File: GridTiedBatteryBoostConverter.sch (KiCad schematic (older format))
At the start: 58 parts, among them J101 Battery Connection, J103 Solar Panels, Q101 IXFP36N20X3, Q102 BC847B-13-F, Q103 SSM3K329R, Q104 SSM3J334R, U101 OPA2837IDGKR, U102 UCC2800DTR

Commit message: Replaced TK32A12N1,S4X TO-220 Toshiba transistors that were use for turning the charger on and off, with a pair of IRFP4321PBF's from Infinion, in a TO-247AC package.  The reson for the change was this part of the circuit carries ~20A at 102.2V peak, so for a 30 degree rise in trace temp with 2 Once copper we need 5mm trace width, but we also need 1.1mm clearance, and this was differcult to acheive with the to-220 package, with out bending the legs etc. These devices are 2 time the price at about  with 15.5 mOhm vs 11 mOhm rds on.  Increased the main FETs gate drive trace to 2mm from 1mm.
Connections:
- net GateDrive: now reaches Q101.1 (G), R113.1
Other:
- moved on the sheet: R113
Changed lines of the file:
@@
 L Device:R R113
 U 1 1 5E4A4E55
-P 5650 2500
-F 0 "R113" H 5720 2546 50  0000 L CNN
-F 1 "10R 1%" H 5720 2455 50  0000 L CNN
-F 2 "Resistors_SMD:R_0805_HandSoldering" V 5580 2500 50  0001 C CNN
-F 3 "https://www.yageo.com/upload/media/product/productsearch/datasheet/rchip/PYu-RC_Group_51_RoHS_L_11.pdf" H 5650 2500 50  0001 C CNN
-F 4 "Yageo" H 0   0   50  0001 C CNN "MFR"
-F 5 "RC0805FR-0710RL" H 0   0   50  0001 C CNN "MPN"
-F 6 "digikey" H 0   0   50  0001 C CNN "SPR"
-F 7 "311-10.0CRCT-ND" H 0   0   50  0001 C CNN "SPN"
-F 8 "-" H 0   0   50  0001 C CNN "SPURL"
-	1    5650 2500
+P 5650 2900
+F 0 "R113" H 5720 2946 50  0000 L CNN
+F 1 "10R 1%" H 5720 2855 50  0000 L CNN
+F 2 "Resistors_SMD:R_0805_HandSoldering" V 5580 2900 50  0001 C CNN
+F 3 "https://www.yageo.com/upload/media/product/productsearch/datasheet/rchip/PYu-RC_Group_51_RoHS_L_11.pdf" H 5650 2900 50  0001 C CNN
+F 4 "Yageo" H 0   400 50  0001 C CNN "MFR"
+F 5 "RC0805FR-0710RL" H 0   400 50  0001 C CNN "MPN"
+F 6 "digikey" H 0   400 50  0001 C CNN "SPR"
+F 7 "311-10.0CRCT-ND" H 0   400 50  0001 C CNN "SPN"
+F 8 "-" H 0   400 50  0001 C CNN "SPURL"
+	1    5650 2900
 	1    0    0    -1
 $EndComp
@@
 	5950 2250 5950 3450
 Wire Wire Line
-	5650 4650 5650 2650
+	5650 4650 5650 3050
 Wire Wire Line
 	2600 4850 4050 4850
 Wire Wire Line
-	5650 2350 5650 2050
+	5650 2750 5650 2050
 Wire Wire Line
 	4900 3450 4700 3450
@@
 Connection ~ 7650 2300
 Connection ~ 7850 2300
+Text Label 5650 2450 0    50   ~ 0
+GateDrive
 $EndSCHEMATC

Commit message: Change footprint for the main switching FET to have a bent drain to achieve trace width and clearance requirements.  Fixed a pin numbering miss alignment between schematic and footprint for the isolating transformer. Spoted trace clearance issue on the 230V AC mains input into the isolating transformer for the house voltage sense, increased to 2.5mm.
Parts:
- Q101: footprint Transistors_ThroughHole_jl:TO-220 -> Transistors_ThroughHole_jl:TO-220_Horizontal_Offset_Drain
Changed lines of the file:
@@
 F 0 "Q101" H 6054 2096 50  0000 L CNN
 F 1 "IXFP36N20X3" H 6054 2005 50  0000 L CNN
-F 2 "Transistors_ThroughHole_jl:TO-220" H 6050 2150 50  0001 C CNN
+F 2 "Transistors_ThroughHole_jl:TO-220_Horizontal_Offset_Drain" H 6050 2150 50  0001 C CNN
 F 3 "http://ixapps.ixys.com/DataSheet/DS100846D(IXFY_-FA-FP36N20X3).pdf" H 5850 2050 50  0001 C CNN
 F 4 "IXYS" H 0   0   50  0001 C CNN "MFR"

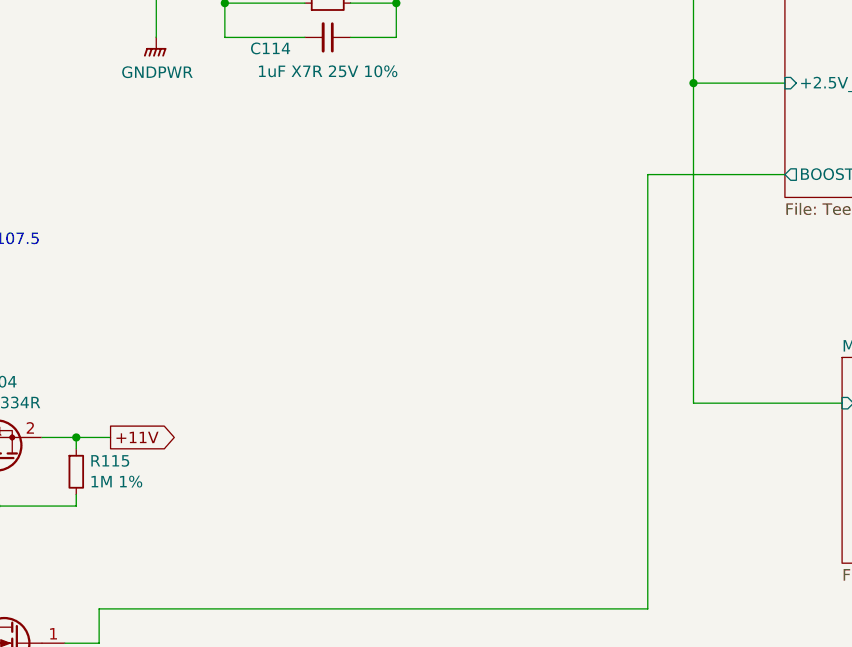
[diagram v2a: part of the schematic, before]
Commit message: Found that my local updates of Kicad footprint librarys, had changed the names of resistor and capacitor footprints, so I updated all these footprint names.  Added circuit to measure the Vin via pin 28 of the Teensy-LC, This will allow the battery system to shut down if the battery voltage gets too low.
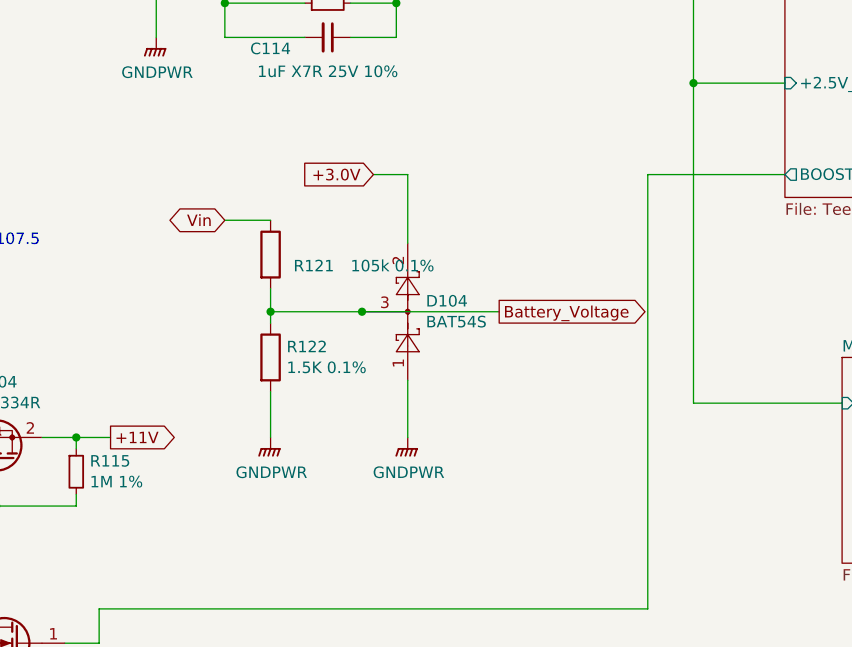
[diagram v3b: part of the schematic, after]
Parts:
- added D104: BAT54S, Package_TO_SOT_SMD:SOT-23_Handsoldering, symbol Diode:BAT54S
- added R121: 105k 0.1%, Resistor_SMD:R_0805_2012Metric_Pad1.15x1.40mm_HandSolder, symbol Device:R
- added R122: 1.5K 0.1%, Resistor_SMD:R_0805_2012Metric_Pad1.15x1.40mm_HandSolder, symbol Device:R
- C101: footprint Capacitors_ThroughHole:CP_Radial_D22.0mm_P10.00mm_SnapIn -> Capacitor_THT:CP_Radial_D22.0mm_P10.00mm_SnapIn
- C103: footprint Capacitors_ThroughHole:CP_Radial_D35.0mm_P10.00mm_SnapIn -> Capacitor_THT:CP_Radial_D35.0mm_P10.00mm_SnapIn
- C105, C106, C107, C108, C109, C110, C111, C112, C113, C114, C115, Cint101, Crolloff101, Ct101: footprint Capacitors_SMD:C_0805_HandSoldering -> Capacitor_SMD:C_0805_2012Metric_Pad1.15x1.40mm_HandSolder
- R101, R102, R103, R104, R105, R106, R107, R108, R109, R110, R111, R112, R113, R115, R116, R117, R118, R119, Rint1, Rint2, Rt101: footprint Resistors_SMD:R_0805_HandSoldering -> Resistor_SMD:R_0805_2012Metric_Pad1.15x1.40mm_HandSolder
- R114, R120: footprint Resistors_SMD:R_1210_HandSoldering -> Resistor_SMD:R_1210_3225Metric_Pad1.42x2.65mm_HandSolder
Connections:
- net +3.0V: now also D104.2
- net 0: now also D104.1, R122.2
- net Vin: now also R121.1
- new net Battery_Voltage: D104.3, R121.2, R122.1

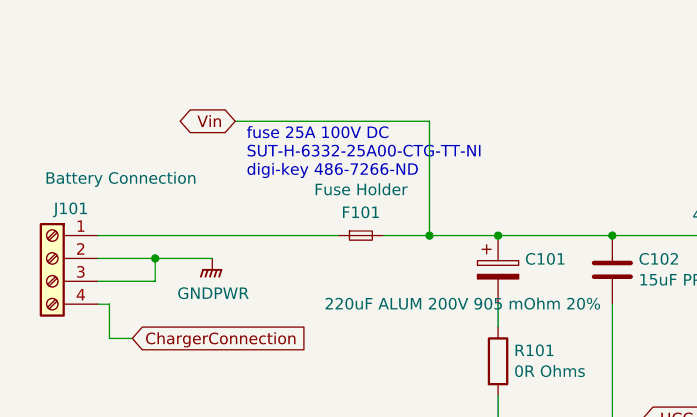
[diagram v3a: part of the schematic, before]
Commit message: Added a dedicated fuse for the charger connection.  Lowered the fuses from 25A to 20A after looking more closely at the data sheet.  Charger is 19.5A atmost and Battery current draw at 80% efficency, 86.8V, 1000W is 14.4A. Reduced the voltage divider resistance for the MainPowerMonitor from 2x 10K to 2x 1K, the reason for this is to draw 1.25mA from the 3.0V supply to increase its effectiveness as input protection for the micro inputs, the BAT54S diodes connect to the 3.0V power supplys so will conduct to this if the input risees a diode drop above 3.0V, so the more current draw from this supply the more it can sink without rising.
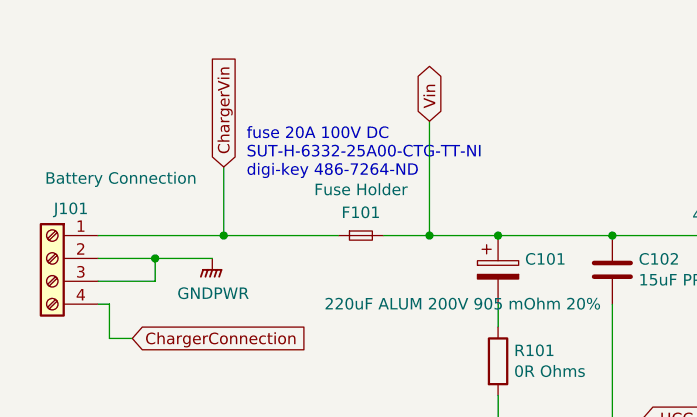
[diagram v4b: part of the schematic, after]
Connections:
- net ChargerVin: now reaches F101.1, J101.1 (Pin_1)
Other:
- note added: "fuse 20A 100V DC\nSUT-H-6332-25A00-CTG-TT-NI\ndigi-key 486-7264-ND"
- note removed: "fuse 25A 100V DC\nSUT-H-6332-25A00-CTG-TT-NI\ndigi-key 486-7266-ND"
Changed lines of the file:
@@
+	1    0    0    -1
+$EndComp
+$Comp
+L Device:R R122
+U 1 1 5F4C1E3E
+P 7600 5400
+F 0 "R122" H 7670 5446 50  0000 L CNN
+F 1 "1.5K 0.1%" H 7670 5355 50  0000 L CNN
+F 2 "Resistor_SMD:R_0805_2012Metric_Pad1.15x1.40mm_HandSolder" V 7530 5400 50  0001 C CNN
+F 3 "https://industrial.panasonic.com/cdbs/www-data/pdf/RDM0000/AOA0000C307.pdf" H 7600 5400 50  0001 C CNN
+F 4 "Panasonic Electronic Components" H 6800 -1100 50  0001 C CNN "MFR"
+F 5 "ERA-6AEB152V" H 6800 -1100 50  0001 C CNN "MPN"
+F 6 "digikey" H 6800 -1100 50  0001 C CNN "SPR"
+F 7 "P1.5KDACT-ND" H 6800 -1100 50  0001 C CNN "SPN"
+F 8 "-" H 6800 -1100 50  0001 C CNN "SPURL"
+	1    7600 5400
+	1    0    0    -1
+$EndComp
+$Comp
+L power:GNDPWR #PWR0116
+U 1 1 5F4C480C
+P 7600 5750
+F 0 "#PWR0116" H 7600 5550 50  0001 C CNN
+F 1 "GNDPWR" H 7604 5596 50  0000 C CNN
+F 2 "" H 7600 5700 50  0001 C CNN
+F 3 "" H 7600 5700 50  0001 C CNN
+	1    7600 5750
+	1    0    0    -1
+$EndComp
+$Comp
+L Device:R R121
+U 1 1 5F4D36B5
+P 7600 4950
+AR Path="/5F4D36B5" Ref="R121"  Part="1"
+AR Path="/5EBD6442/5F4D36B5" Ref="R?"  Part="1"
+F 0 "R121" H 7700 4900 50  0000 L CNN
+F 1 "105k 0.1%" H 7950 4900 50  0000 L CNN
+F 2 "Resistor_SMD:R_0805_2012Metric_Pad1.15x1.40mm_HandSolder" V 7530 4950 50  0001 C CNN
+F 3 "https://industrial.panasonic.com/cdbs/www-data/pdf/RDM0000/AOA0000C307.pdf" H 7600 4950 50  0001 C CNN
+F 4 "Panasonic Electronic Components" H -700 3950 50  0001 C CNN "MFR"
+F 5 "ERA-6AEB1053V" H -700 3950 50  0001 C CNN "MPN"
+F 6 "digikey" H -700 3950 50  0001 C CNN "SPR"
+F 7 "P105KDACT-ND" H -700 3950 50  0001 C CNN "SPN"
+F 8 "-" H -700 3950 50  0001 C CNN "SPURL"
+	1    7600 4950
+	1    0    0    -1
+$EndComp
+$Comp
+L Diode:BAT54S D?
+U 1 1 5F53D777
+P 8200 5200
+AR Path="/5F15BF3C/5F53D777" Ref="D?"  Part="1"
+AR Path="/5F53D777" Ref="D104"  Part="1"
+F 0 "D104" V 8246 5279 50  0000 L CNN
+F 1 "BAT54S" V 8155 5279 50  0000 L CNN
+F 2 "Package_TO_SOT_SMD:SOT-23_Handsoldering" H 8200 4700 50  0001 C CNN
+F 3 "http://toshiba.semicon-storage.com/info/docget.jsp?did=37137&prodName=TBAT54" H 8200 5200 50  0001 C CNN
+F 4 "Toshiba Semiconductor and Storage" H 3900 -1650 50  0001 C CNN "MFR"
+F 5 "TBAT54S,LM" H 3900 -1650 50  0001 C CNN "MPN"
+F 6 "digikey" H 3900 -1650 50  0001 C CNN "SPR"
+F 7 "TBAT54SLMCT-ND" H 3900 -1650 50  0001 C CNN "SPN"
+F 8 "-" H 3900 -1650 50  0001 C CNN "SPURL"
+	1    8200 5200
+	0    1    -1   0
+$EndComp
+$Comp
+L power:GNDPWR #PWR0117
+U 1 1 5F565480
+P 8200 5750
+F 0 "#PWR0117" H 8200 5550 50  0001 C CNN
+F 1 "GNDPWR" H 8204 5596 50  0000 C CNN
+F 2 "" H 8200 5700 50  0001 C CNN
+F 3 "" H 8200 5700 50  0001 C CNN
+	1    8200 5750
 	1    0    0    -1
 $EndComp
@@
 Text GLabel 800  5250 2    50   Output ~ 0
 Vboost_out
-Text GLabel 1450 1200 0    50   BiDi ~ 0
+Text GLabel 2300 1200 1    50   BiDi ~ 0
 Vin
 Text GLabel 6900 5750 2    50   Output ~ 0
@@
 +2.5V_REF
 Text Notes 1500 1450 0    50   ~ 0
-fuse 25A 100V DC\nSUT-H-6332-25A00-CTG-TT-NI\ndigi-key 486-7266-ND
+fuse 20A 100V DC\nSUT-H-6332-25A00-CTG-TT-NI\ndigi-key 486-7264-ND
+Text Label 5650 2450 0    50   ~ 0
+GateDrive
+Text GLabel 7400 4800 0    50   BiDi ~ 0
+Vin
+Text GLabel 8600 5200 2    50   Output ~ 0
+Battery_Voltage
+Text GLabel 8050 4600 0    50   Input ~ 0
++3.0V
 Wire Wire Line
 	2600 2600 2600 2550
@@
 	6400 6050 6400 6450
 Wire Wire Line
-	1450 1200 2300 1200
-Wire Wire Line
 	2300 1200 2300 1700
 Wire Wire Line
@@
 	4650 5750 4950 5750
 Wire Wire Line
-	850  1700 1900 1700
+	850  1700 1400 1700
 Wire Wire Line
 	2100 1700 2300 1700
@@
 Wire Wire Line
 	7650 2300 7850 2300
+Wire Wire Line
+	7400 4800 7600 4800
+Wire Wire Line
+	7600 5550 7600 5750
+Wire Wire Line
+	8050 4600 8200 4600
+Wire Wire Line
+	8200 4600 8200 4900
+Wire Wire Line
+	8200 5500 8200 5750
+Wire Wire Line
+	7600 5100 7600 5200
+Wire Wire Line
+	8600 5200 8000 5200
+Wire Wire Line
+	8000 5200 7600 5200
+Wire Wire Line
+	7600 5200 7600 5250
 Connection ~ 2600 2550
 Connection ~ 3100 1700
@@
 Connection ~ 7650 2300
 Connection ~ 7850 2300
-Text Label 5650 2450 0    50   ~ 0
-GateDrive
-Text GLabel 7400 4800 0    50   BiDi ~ 0
-Vin
-$Comp
-L Device:R R122
-U 1 1 5F4C1E3E
-P 7600 5400
-F 0 "R122" H 7670 5446 50  0000 L CNN
-F 1 "1.5K 0.1%" H 7670 5355 50  0000 L CNN
-F 2 "Resistor_SMD:R_0805_2012Metric_Pad1.15x1.40mm_HandSolder" V 7530 5400 50  0001 C CNN
-F 3 "https://industrial.panasonic.com/cdbs/www-data/pdf/RDM0000/AOA0000C307.pdf" H 7600 5400 50  0001 C CNN
-F 4 "Panasonic Electronic Components" H 6800 -1100 50  0001 C CNN "MFR"
-F 5 "ERA-6AEB152V" H 6800 -1100 50  0001 C CNN "MPN"
-F 6 "digikey" H 6800 -1100 50  0001 C CNN "SPR"
-F 7 "P1.5KDACT-ND" H 6800 -1100 50  0001 C CNN "SPN"
-F 8 "-" H 6800 -1100 50  0001 C CNN "SPURL"
-	1    7600 5400
-	1    0    0    -1
-$EndComp
-$Comp
-L power:GNDPWR #PWR0116
-U 1 1 5F4C480C
-P 7600 5750
-F 0 "#PWR0116" H 7600 5550 50  0001 C CNN
-F 1 "GNDPWR" H 7604 5596 50  0000 C CNN
-F 2 "" H 7600 5700 50  0001 C CNN
-F 3 "" H 7600 5700 50  0001 C CNN
-	1    7600 5750
-	1    0    0    -1
-$EndComp
-Text GLabel 8600 5200 2    50   Output ~ 0
-Battery_Voltage
-$Comp
-L Device:R R121
-U 1 1 5F4D36B5
-P 7600 4950
-AR Path="/5F4D36B5" Ref="R121"  Part="1"
-AR Path="/5EBD6442/5F4D36B5" Ref="R?"  Part="1"
-F 0 "R121" H 7700 4900 50  0000 L CNN
-F 1 "105k 0.1%" H 7950 4900 50  0000 L CNN
-F 2 "Resistor_SMD:R_0805_2012Metric_Pad1.15x1.40mm_HandSolder" V 7530 4950 50  0001 C CNN
-F 3 "https://industrial.panasonic.com/cdbs/www-data/pdf/RDM0000/AOA0000C307.pdf" H 7600 4950 50  0001 C CNN
-F 4 "Panasonic Electronic Components" H -700 3950 50  0001 C CNN "MFR"
-F 5 "ERA-6AEB1053V" H -700 3950 50  0001 C CNN "MPN"
-F 6 "digikey" H -700 3950 50  0001 C CNN "SPR"
-F 7 "P105KDACT-ND" H -700 3950 50  0001 C CNN "SPN"
-F 8 "-" H -700 3950 50  0001 C CNN "SPURL"
-	1    7600 4950
-	1    0    0    -1
-$EndComp
-Wire Wire Line
-	7400 4800 7600 4800
-Wire Wire Line
-	7600 5550 7600 5750
-Text GLabel 8050 4600 0    50   Input ~ 0
-+3.0V
-$Comp
-L Diode:BAT54S D?
-U 1 1 5F53D777
-P 8200 5200
-AR Path="/5F15BF3C/5F53D777" Ref="D?"  Part="1"
-AR Path="/5F53D777" Ref="D104"  Part="1"
-F 0 "D104" V 8246 5279 50  0000 L CNN
-F 1 "BAT54S" V 8155 5279 50  0000 L CNN
-F 2 "Package_TO_SOT_SMD:SOT-23_Handsoldering" H 8200 4700 50  0001 C CNN
-F 3 "http://toshiba.semicon-storage.com/info/docget.jsp?did=37137&prodName=TBAT54" H 8200 5200 50  0001 C CNN
-F 4 "Toshiba Semiconductor and Storage" H 3900 -1650 50  0001 C CNN "MFR"
-F 5 "TBAT54S,LM" H 3900 -1650 50  0001 C CNN "MPN"
-F 6 "digikey" H 3900 -1650 50  0001 C CNN "SPR"
-F 7 "TBAT54SLMCT-ND" H 3900 -1650 50  0001 C CNN "SPN"
-F 8 "-" H 3900 -1650 50  0001 C CNN "SPURL"
-	1    8200 5200
-	0    1    -1   0
-$EndComp
-Wire Wire Line
-	8050 4600 8200 4600
-Wire Wire Line
-	8200 4600 8200 4900
-$Comp
-L power:GNDPWR #PWR0117
-U 1 1 5F565480
-P 8200 5750
-F 0 "#PWR0117" H 8200 5550 50  0001 C CNN
-F 1 "GNDPWR" H 8204 5596 50  0000 C CNN
-F 2 "" H 8200 5700 50  0001 C CNN
-F 3 "" H 8200 5700 50  0001 C CNN
-	1    8200 5750
-	1    0    0    -1
-$EndComp
-Wire Wire Line
-	8200 5500 8200 5750
-Wire Wire Line
-	7600 5100 7600 5200
-Wire Wire Line
-	8600 5200 8000 5200
-Wire Wire Line
-	8000 5200 7600 5200
 Connection ~ 8000 5200
 Connection ~ 7600 5200
-Wire Wire Line
-	7600 5200 7600 5250
+Text GLabel 1400 1400 1    50   Input ~ 0
+ChargerVin
+Wire Wire Line
+	1400 1400 1400 1700
+Connection ~ 1400 1700
+Wire Wire Line
+	1400 1700 1900 1700
 $EndSCHEMATC

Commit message: Replaced the 3.5mm headphone jack which was used as the current transformer input, I thought due to the dangerous voltages that can be developed if it is connected to the mains without being pluged into the burden resistor located on the board, that it might be better to cut the connector off an wire it to the board, this would also allow for the option of perhapes a 10V zener to be solder accross the outputs of the current sense transformer.
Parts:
- J101: footprint digikey-footprints:Term_Block_1x4_P5mm -> Connect_jl:PhoenixContact_1x4_P5mm
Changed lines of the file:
@@
 F 0 "J101" H 568 2017 50  0000 C CNN
 F 1 "Battery Connection" H 350 2150 50  0000 C CNN
-F 2 "digikey-footprints:Term_Block_1x4_P5mm" H 650 1800 50  0001 C CNN
+F 2 "Connect_jl:PhoenixContact_1x4_P5mm" H 650 1800 50  0001 C CNN
 F 3 "https://www.phoenixcontact.com/pxc-oc-itemdetail-pdf-web/eshop?lineItemType=LineItem&UID=1935792" H 650 1800 50  0001 C CNN
 F 4 "Phoenix Contact" H 0   0   50  0001 C CNN "MFR"

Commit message: Added voltage divider network and input protection to measure, the Solar input voltage, I decided this would be usefull in the cases where the solar is producing voltage over 160V, but the house is stillimporting power from the Grid, there is not point in powering up the boost converter because we can't get power into the system, as output is 160V.  Also update the TestPoint footprints to match the latest Kicad naming convention, simular to my resistor and capacitor footprint changes a few commits ago.
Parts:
- TP101, TP102, TP103: footprint Measurement_Points:Measurement_Point_Square-SMD-Pad_Big -> TestPoint:TestPoint_Pad_3.0x3.0mm
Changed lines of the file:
@@
 F 0 "TP101" H 1508 6418 50  0000 L CNN
 F 1 "TestPoint" H 1508 6327 50  0000 L CNN
-F 2 "Measurement_Points:Measurement_Point_Square-SMD-Pad_Big" H 1650 6300 50  0001 C CNN
+F 2 "TestPoint:TestPoint_Pad_3.0x3.0mm" H 1650 6300 50  0001 C CNN
 F 3 "~" H 1650 6300 50  0001 C CNN
 F 4 "-" H 0   0   50  0001 C CNN "MFR"
@@
 F 0 "TP102" V 3754 2938 50  0000 L CNN
 F 1 "TestPoint" V 3845 2938 50  0000 L CNN
-F 2 "Measurement_Points:Measurement_Point_Square-SMD-Pad_Big" H 4000 2750 50  0001 C CNN
+F 2 "TestPoint:TestPoint_Pad_3.0x3.0mm" H 4000 2750 50  0001 C CNN
 F 3 "~" H 4000 2750 50  0001 C CNN
 F 4 "-" H 0   0   50  0001 C CNN "MFR"
@@
 F 0 "TP103" H 4758 3068 50  0000 L CNN
 F 1 "TestPoint" H 4758 2977 50  0000 L CNN
-F 2 "Measurement_Points:Measurement_Point_Square-SMD-Pad_Big" H 4900 2950 50  0001 C CNN
+F 2 "TestPoint:TestPoint_Pad_3.0x3.0mm" H 4900 2950 50  0001 C CNN
 F 3 "~" H 4900 2950 50  0001 C CNN
 F 4 "-" H 0   0   50  0001 C CNN "MFR"

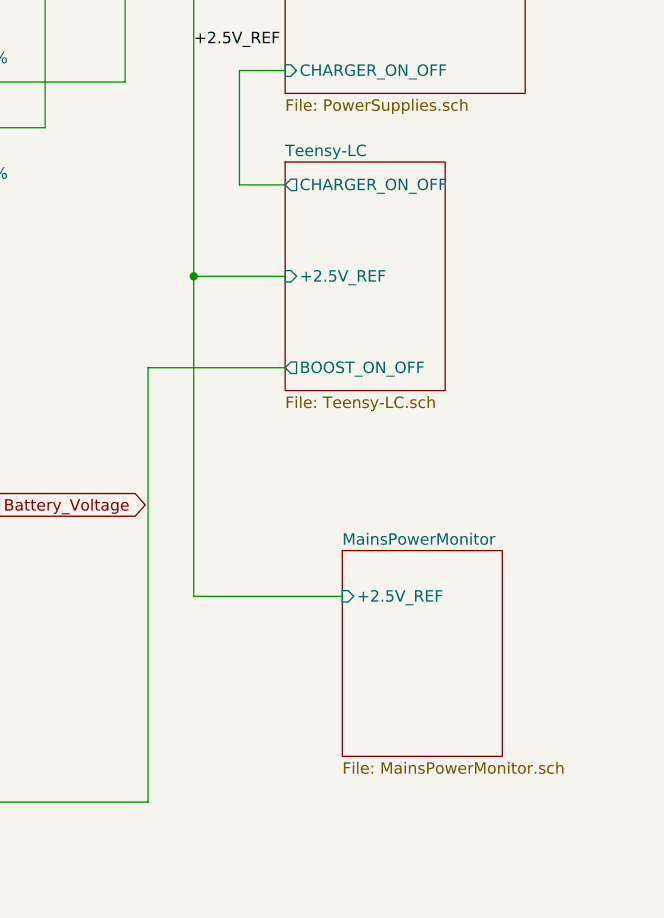
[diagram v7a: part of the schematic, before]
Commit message: Added Current_Range_Hi_Lo signal from the Mains Current Sense circuit to the Micro so we can tell what range we are operating on.
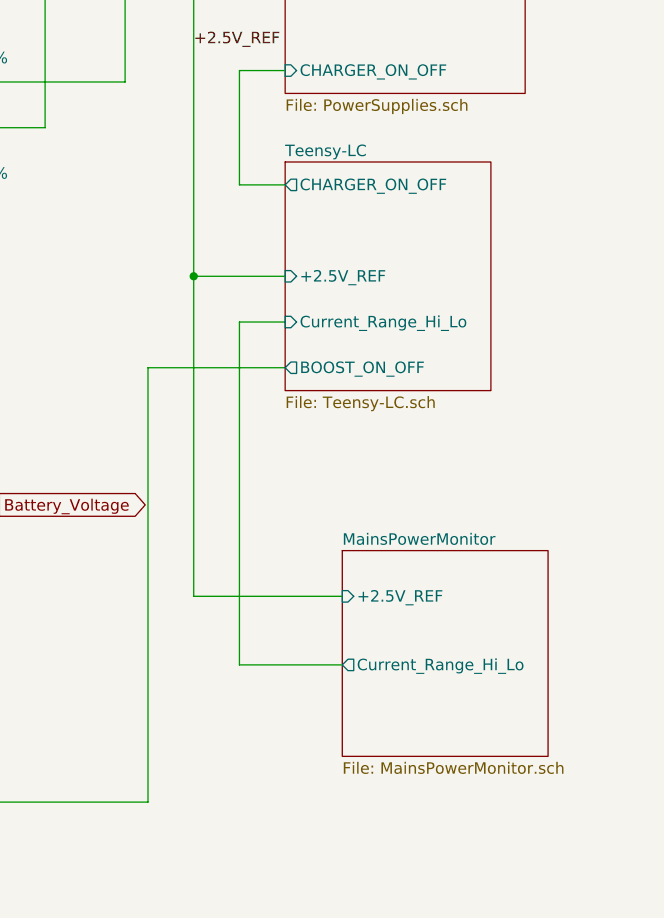
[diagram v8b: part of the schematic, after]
